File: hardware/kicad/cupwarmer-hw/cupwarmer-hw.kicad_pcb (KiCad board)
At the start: 4 copper layers, 56 x 56 mm, 48 parts, among them J1 I2C Service, J2 THERM_MON, J3 STATUS_MON, Q1 AO3400 SOT-23, U1 STWLC38JRM

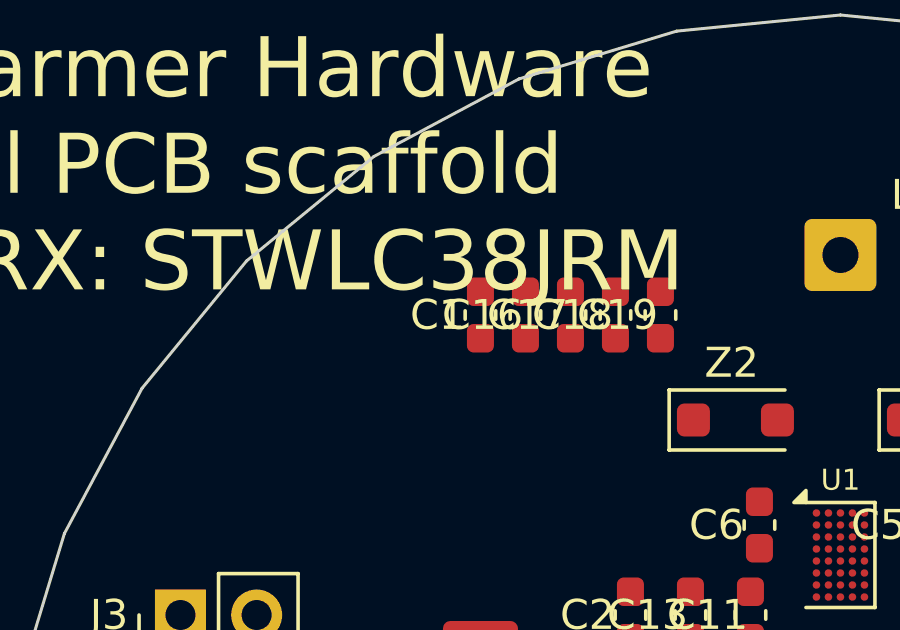
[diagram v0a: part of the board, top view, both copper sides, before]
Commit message: Swap Cs primary caps to C0G 1206 (3x100nF GRM31C5C1H104JA01L)
C1/C16/C17 were 100nF/50V X7R 0603 (Würth 885012206095). cup warmer is
in continuous warm operation (heater H1 + coil losses), so the X7R
temperature drift (+/-15%) plus DC bias capacitance loss would shift
the AC series resonance and degrade efficiency / VRECT regulation.
C0G (NP0, +/-30 ppm/degC, no DC-bias drop) is required.

JLC DB confirmed 100nF/50V C0G is unavailable in 0603 and 0805
(C0G volumetric efficiency caps 0805 50V at ~33nF). 1206 is the
smallest stocked size for 100nF/50V C0G; 3x1206 (15.4 mm^2) beats
14x22nF/0805 (35 mm^2) on total board area, so going up in package
size for fewer parts is the right trade-off here.

Footprint pitch widened from 1.5 mm to 2.5 mm to clear 1206 courtyards
(C1@85.5/82, C16@88/82, C17@90.5/82, all rotation 90, C18/C19 retained
at 92.5/94). DRC violation count drops from 231 to 212 with the three
courtyards_overlap entries for C1/C16/C17 cleared. Net topology
preserved (verified via netlist diff: Net-(C1-Pad1)=L1.2+caps,
Net-(C1-Pad2)=U1.AC1+caps unchanged). C18/C19 (10nF NP0 0603) and
unrelated 885012206095 instances (C4/C22/C24 bypass caps) untouched.

Co-Authored-By: Claude Opus 4.7 (1M context) <noreply@anthropic.com>
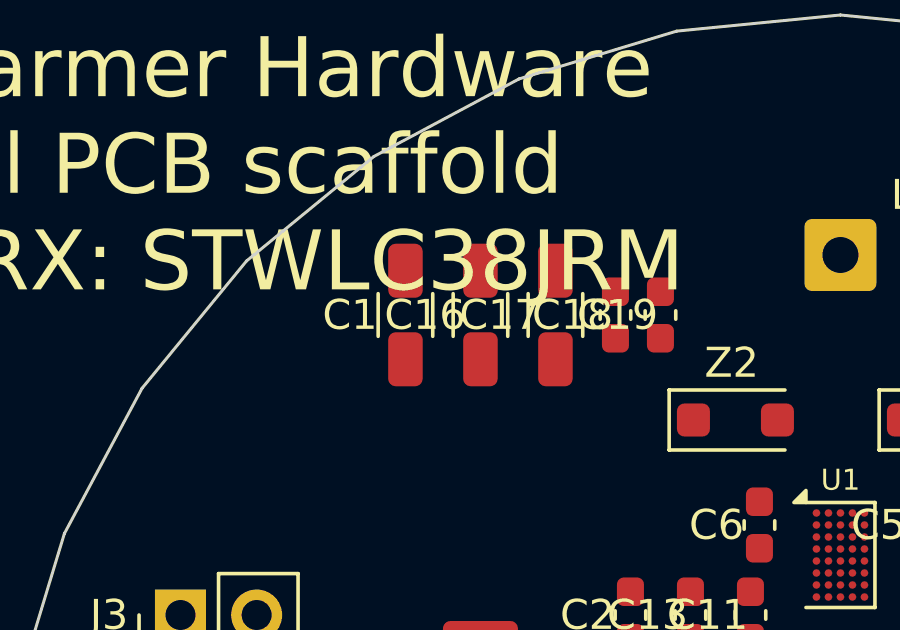
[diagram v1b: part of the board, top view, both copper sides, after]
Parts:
- C1, C16, C17: footprint Capacitor_SMD:C_0603_1608Metric -> Capacitor_SMD:C_1206_3216Metric
- moved C1 2.50 mm to (85.5, 82.0)
- moved C16 1.50 mm to (88.0, 82.0)
- moved C17 0.50 mm to (90.5, 82.0)

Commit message: Sync TH2 silk Value to 100k NCP18WF104F12RB
PCB silk on TH2 read "NTC 10k B3950" — drift from an earlier candidate
that was never reflected in sch/BOM. STWLC38 NTC RX_NTC reference per
UM3154 §9.1.7 (and STEVAL-WLC38RX BOM) is R7=10k pull-up + TH2=100k
NCP18WF104F12RB B25/85=4250K, which is what sch and BOM have already.
silk-only fix; no schematic, BOM, or net change.

trip-temperature numerical sizing (R7 vs NTC value vs default 0x40
threshold) is deferred to Phase 1.4 (NTC divider redesign) of
docs/plans/20260505-um3154-section9-board-fixes.md.

Co-Authored-By: Claude Opus 4.7 (1M context) <noreply@anthropic.com>
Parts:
- TH2: value NTC 10k B3950 -> NTC 100k B4250
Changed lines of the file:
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@@
 			)
 		)
-		(property "Value" "NTC 10k B3950"
+		(property "Value" "NTC 100k B4250"
 			(at 0 1.43 0)
 			(layer "F.Fab")
